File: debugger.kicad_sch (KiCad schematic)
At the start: 15 parts, among them J10 TC_SWD, J6 MCU_SWD, U6 ATSAMD11

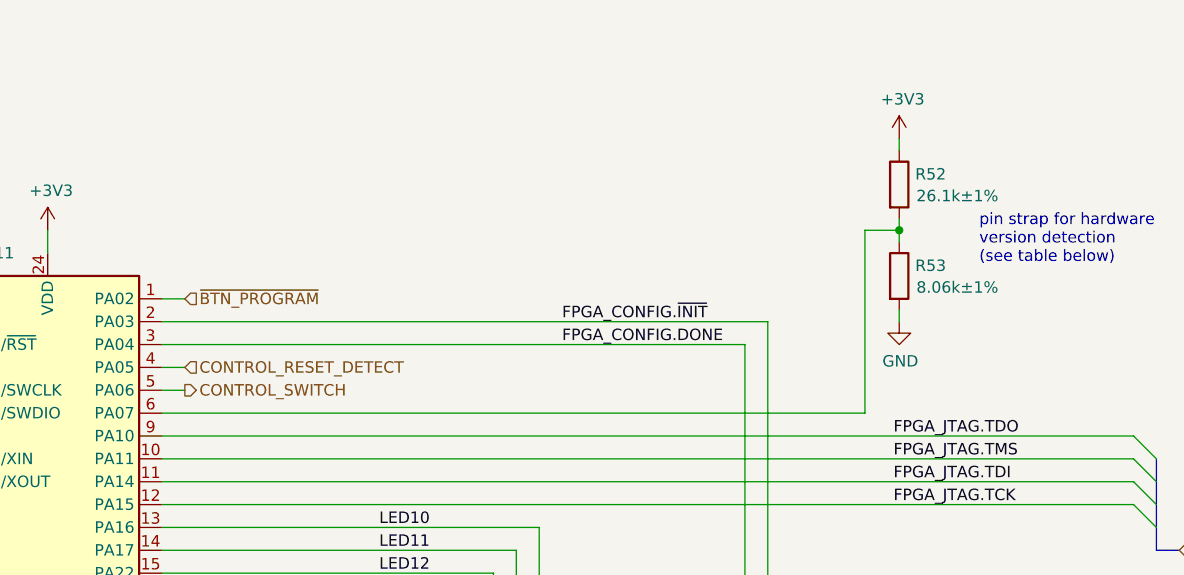
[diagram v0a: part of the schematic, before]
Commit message: Upgrade to KiCad 7
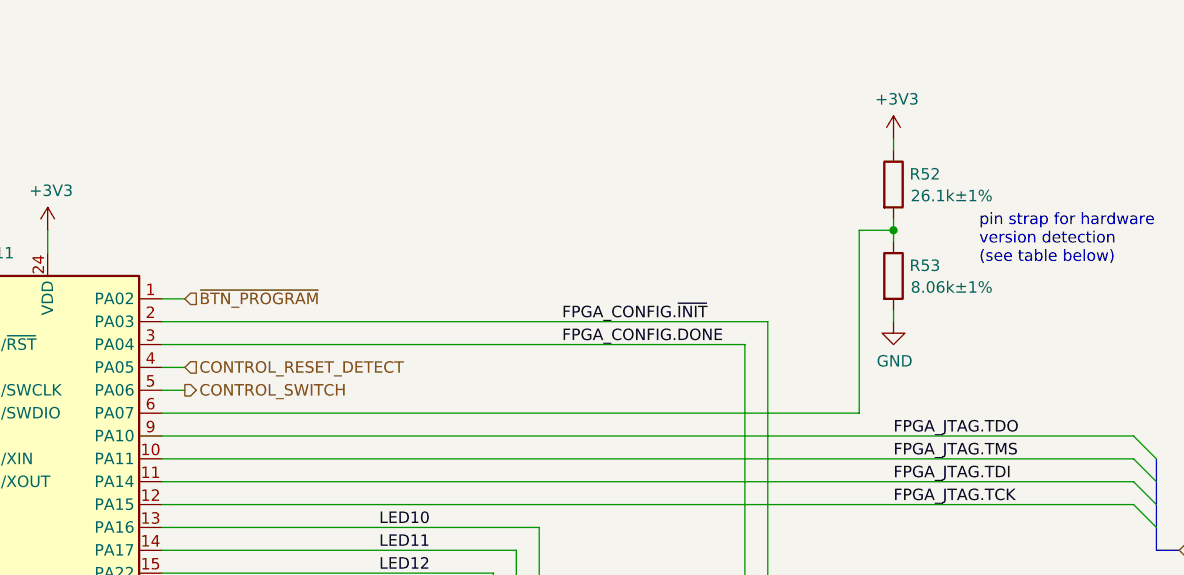
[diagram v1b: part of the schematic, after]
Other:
- moved on the sheet: R52, R53

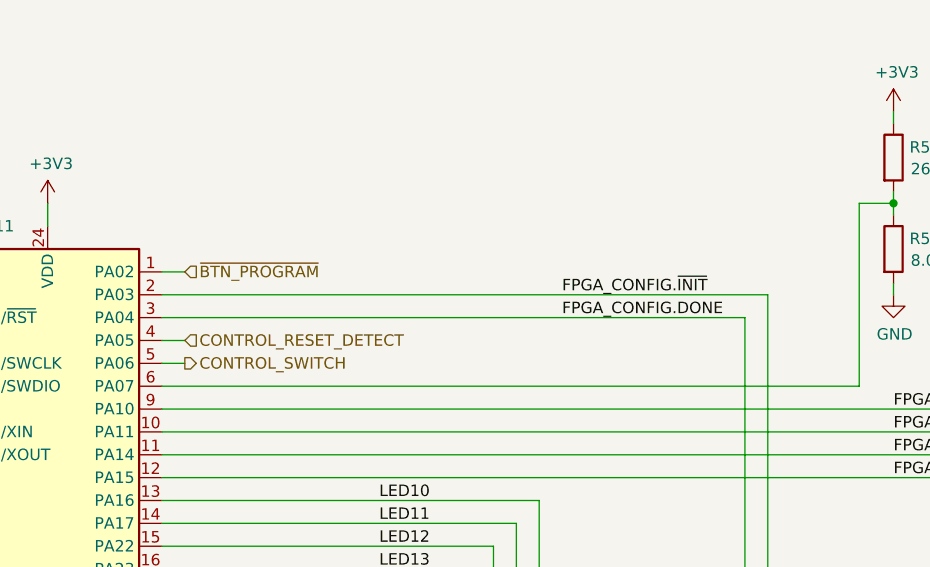
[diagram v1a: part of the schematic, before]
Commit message: Add FPGA_INIT (INITN) series resistor
Fixes #14
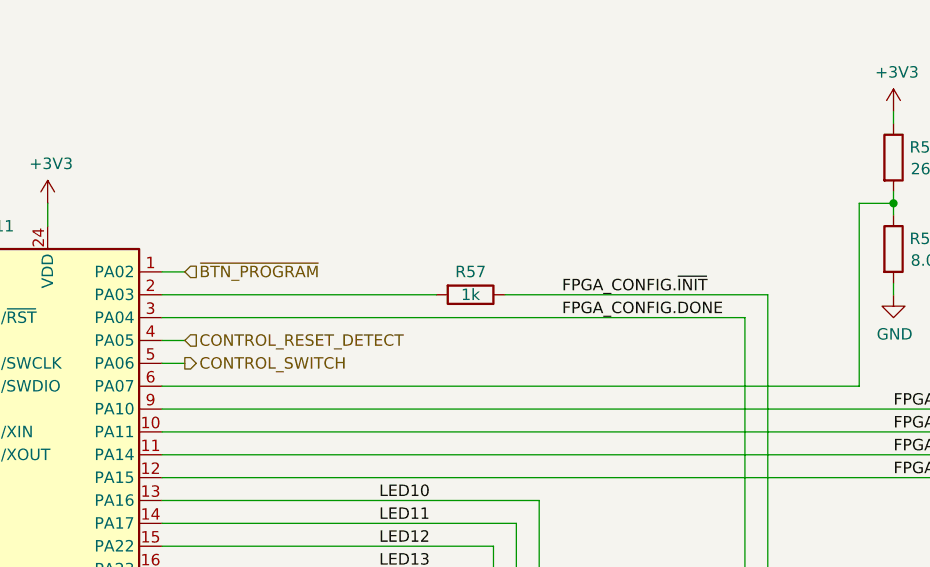
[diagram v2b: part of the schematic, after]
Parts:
- added R57: 1k, Resistor_SMD:R_0402_1005Metric, symbol Device:R
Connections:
- net FPGA_CONFIG.~{INIT}: now also R57.1; no longer U6.2 (PA03)
- new net: R57.2, U6.2 (PA03)
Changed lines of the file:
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@@
-    (stroke (width 0) (type default))
-  )
-  (wire (pts (xy 137.16 62.23) (xy 204.47 62.23))
     (stroke (width 0) (type default))
   )
@@
     (stroke (width 0) (type default))
   )
+  (wire (pts (xy 175.26 62.23) (xy 204.47 62.23))
+    (stroke (width 0) (type default))
+  )
   (wire (pts (xy 50.8 45.72) (xy 50.8 48.26))
     (stroke (width 0) (type default))
@@
   )
   (wire (pts (xy 60.96 48.26) (xy 63.5 48.26))
+    (stroke (width 0) (type default))
+  )
+  (wire (pts (xy 137.16 62.23) (xy 167.64 62.23))
     (stroke (width 0) (type default))
   )
@@
         )
       )
+    )
+  )
+  (symbol (lib_id "Device:R") (at 171.45 62.23 270) (unit 1)
+    (in_bom yes) (on_board yes) (dnp no)
+    (property "Reference" "R57" (at 171.45 59.69 90)
+      (effects (font (size 1.27 1.27)))
+    )
+    (property "Value" "1k" (at 171.45 62.23 90)
+      (effects (font (size 1.27 1.27)))
+    )
+    (property "Footprint" "Resistor_SMD:R_0402_1005Metric" (at 171.45 60.452 90)
+      (effects (font (size 1.27 1.27)) hide)
+    )
+    (property "Datasheet" "~" (at 171.45 62.23 0)
+      (effects (font (size 1.27 1.27)) hide)
+    )
+    (property "Part Number" "RC0402JR-071KL" (at 171.45 62.23 0)
+      (effects (font (size 1.27 1.27)) hide)
+    )
+    (property "Substitution" "any equivalent" (at 171.45 62.23 0)
+      (effects (font (size 1.27 1.27)) hide)
+    )
+    (property "Description" "RES 1K OHM 5% 1/16W 0402" (at 171.45 62.23 0)
+      (effects (font (size 1.27 1.27)) hide)
+    )
+    (property "Manufacturer" "Yageo" (at 171.45 62.23 0)
+      (effects (font (size 1.27 1.27)) hide)
+    )
+    (pin "1")
+    (pin "2")
+    (instances
+      (project "cynthion"
+        (path "/fb621148-8145-4217-9712-738e1b5a4823/00000000-0000-0000-0000-00005dddb747"
+          (reference "R57") (unit 1)
+        )
+        (path "/fb621148-8145-4217-9712-738e1b5a4823/00000000-0000-0000-0000-00005dcaa6d2"
+          (reference "R118") (unit 1)
+        )
+      )

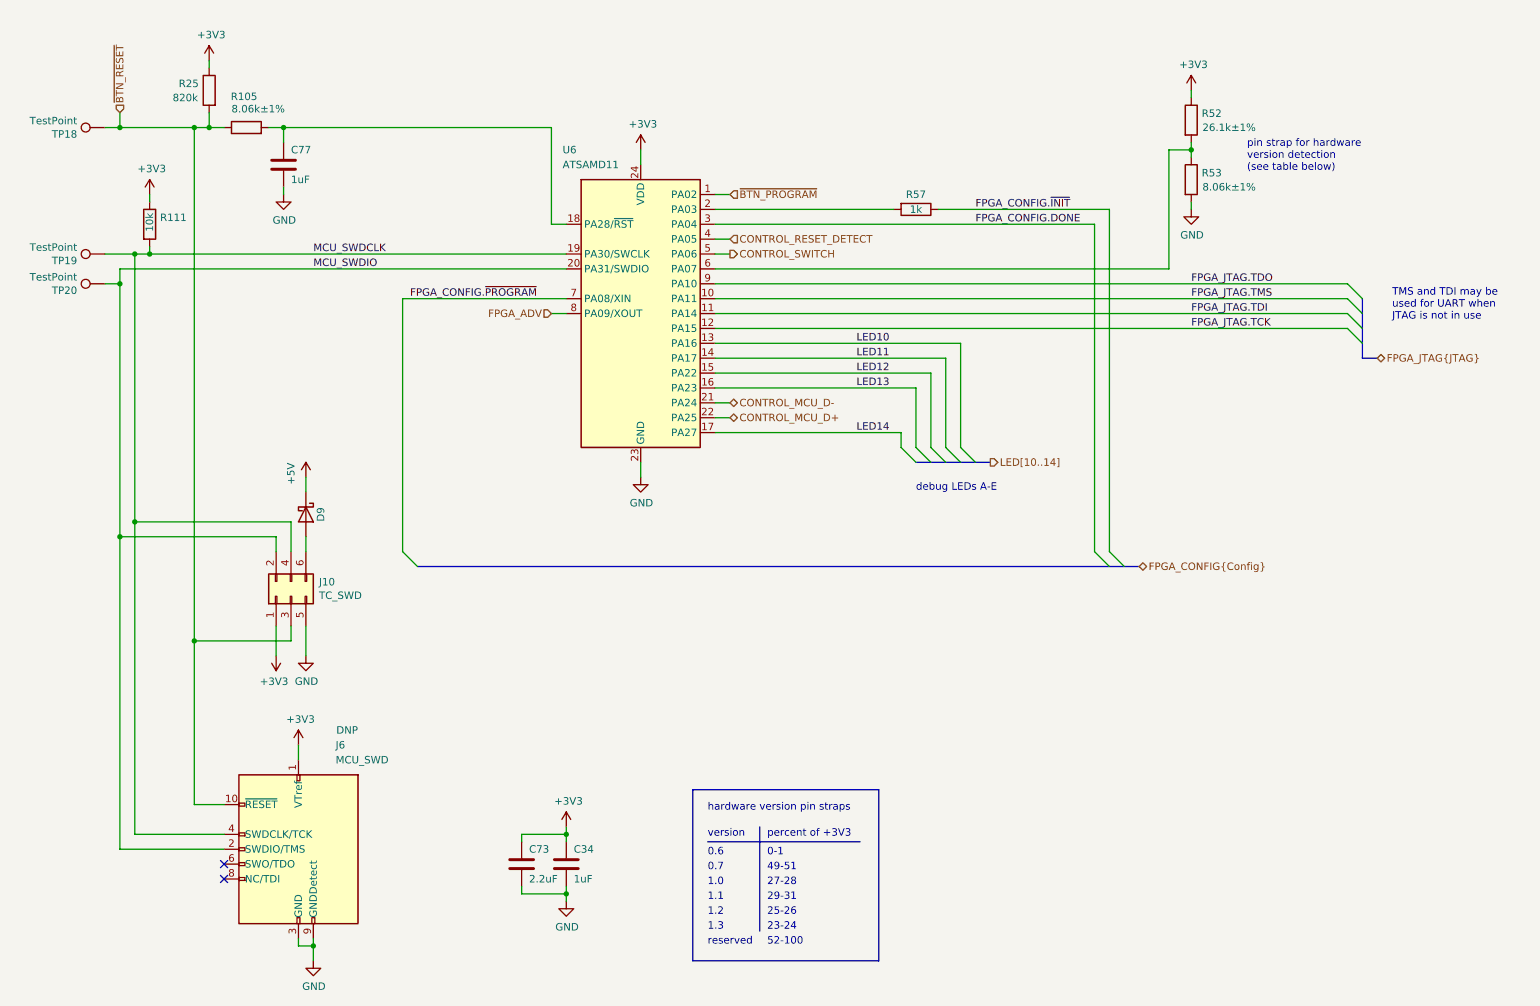
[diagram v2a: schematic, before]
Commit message: Clean up schematic
- Renumber Pmod signal names to match silkscreen labels
- Clean up FPGA symbol
- Clean up PHY symbol
- Add title block to newer sheets
- Fix horizontal line in LED sheet
- Improve various label positions
- Update data sheet fields
- Renumber pages
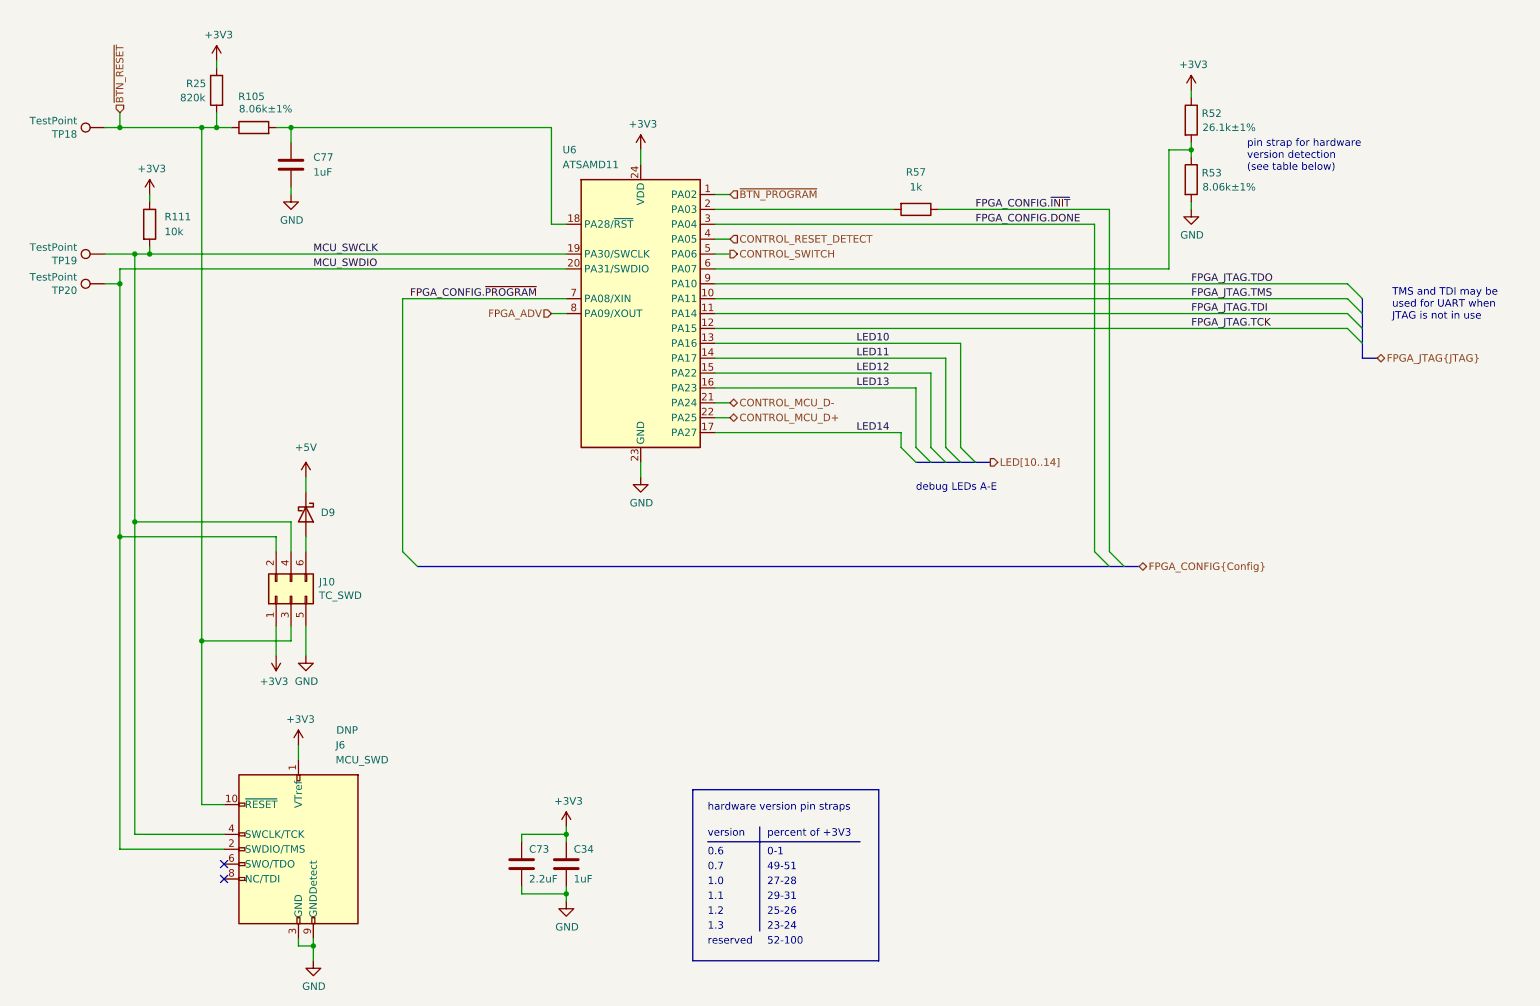
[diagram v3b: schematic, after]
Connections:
- net MCU_SWDCLK renamed MCU_SWCLK
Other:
- moved on the sheet: C77, R105, R25

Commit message: Update version detection pin strap
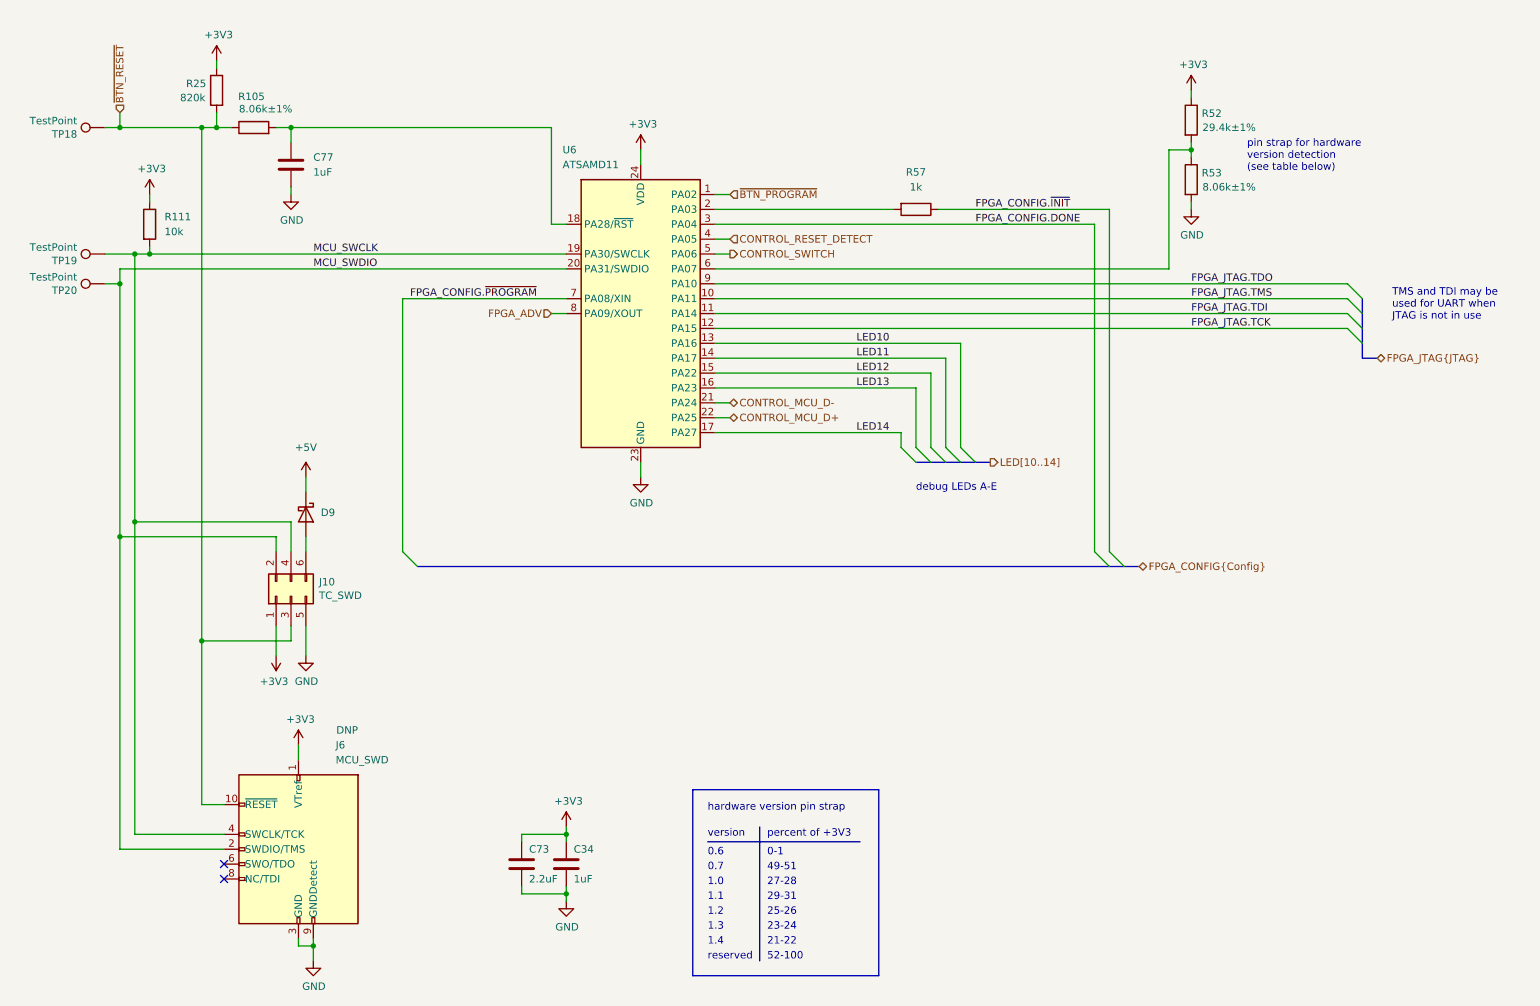
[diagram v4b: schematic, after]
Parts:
- R52: value 26.1k±1% -> 29.4k±1%; Part Number RC0402FR-0726K1L -> RC0402FR-0729K4L
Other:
- note added: "1.4"
- note added: "21-22"
- note added: "hardware version pin strap"
- note removed: "hardware version pin straps"
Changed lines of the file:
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@@
     (stroke (width 0) (type default))
   )
-  (polyline (pts (xy 133.35 161.29) (xy 133.35 190.5))
+  (polyline (pts (xy 133.35 161.29) (xy 133.35 193.04))
     (stroke (width 0) (type default))
   )
@@
     (stroke (width 0) (type default))
   )
-  (polyline (pts (xy 165.1 161.29) (xy 165.1 190.5))
+  (polyline (pts (xy 165.1 161.29) (xy 165.1 193.04))
     (stroke (width 0) (type default))
   )
@@
     (stroke (width 0) (type default))
   )
-  (polyline (pts (xy 165.1 190.5) (xy 133.35 190.5))
+  (polyline (pts (xy 165.1 193.04) (xy 133.35 193.04))
     (stroke (width 0) (type default))
   )
@@
     (stroke (width 0) (type default))
   )
-  (polyline (pts (xy 144.78 167.64) (xy 144.78 185.42))
+  (polyline (pts (xy 144.78 167.64) (xy 144.78 190.5))
     (stroke (width 0) (type default))
   )
@@
     (stroke (width 0) (type default))
   )
+  (text "1.4" (at 135.89 187.96 0)
+    (effects (font (size 1.27 1.27)) (justify left bottom))
+  )
   (text "debug LEDs A-E" (at 171.45 110.49 0)
     (effects (font (size 1.27 1.27)) (justify left bottom))
   )
-  (text "reserved" (at 135.89 187.96 0)
+  (text "reserved" (at 135.89 190.5 0)
     (effects (font (size 1.27 1.27)) (justify left bottom))
   )
@@
     (effects (font (size 1.27 1.27)) (justify left bottom))
   )
-  (text "52-100" (at 146.05 187.96 0)
+  (text "52-100" (at 146.05 190.5 0)
     (effects (font (size 1.27 1.27)) (justify left bottom))
   )
@@
     (effects (font (size 1.27 1.27)) (justify left bottom))
   )
+  (text "21-22" (at 146.05 187.96 0)
+    (effects (font (size 1.27 1.27)) (justify left bottom))
+  )
   (text "1.1" (at 135.89 180.34 0)
     (effects (font (size 1.27 1.27)) (justify left bottom))
   )
-  (text "hardware version pin straps" (at 135.89 165.1 0)
+  (text "hardware version pin strap" (at 135.89 165.1 0)
     (effects (font (size 1.27 1.27)) (justify left bottom))
   )
@@
       (effects (font (size 1.27 1.27)) (justify left))
     )
-    (property "Value" "26.1k±1%" (at 220.345 48.26 0)
+    (property "Value" "29.4k±1%" (at 220.345 48.26 0)
       (effects (font (size 1.27 1.27)) (justify left))
     )
@@
       (effects (font (size 1.27 1.27)) hide)
     )
-    (property "Part Number" "RC0402FR-0726K1L" (at 218.44 46.99 0)
+    (property "Part Number" "RC0402FR-0729K4L" (at 218.44 46.99 0)
       (effects (font (size 1.27 1.27)) hide)
     )
@@
       (effects (font (size 1.27 1.27)) hide)
     )
-    (property "Description" "RES 26.1K OHM 1% 1/16W 0402" (at 218.44 46.99 0)
-      (effects (font (size 1.27 1.27)) hide)
-    )
+    (property "Description" "RES 29.4K OHM 1% 1/16W 0402" (at 218.44 46.99 0)
+      (effects (font (size 1.27 1.27)) hide)
+    )

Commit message: opened and saved in KiCad 7.0.10
after upgrading from 7.0.9
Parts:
- renumbered R57 to R118
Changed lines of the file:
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@@
   (symbol (lib_id "Device:R") (at 171.45 62.23 270) (unit 1)
     (in_bom yes) (on_board yes) (dnp no) (fields_autoplaced)
-    (property "Reference" "R57" (at 171.45 55.88 90)
+    (property "Reference" "R118" (at 171.45 55.88 90)
       (effects (font (size 1.27 1.27)))
     )
@@
     (instances
       (project "cynthion"
-        (path "/fb621148-8145-4217-9712-738e1b5a4823/00000000-0000-0000-0000-00005dddb747"
-          (reference "R57") (unit 1)
-        )
         (path "/fb621148-8145-4217-9712-738e1b5a4823/00000000-0000-0000-0000-00005dcaa6d2"
           (reference "R118") (unit 1)

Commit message: Update copyright notices
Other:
- company: Copyright 2019-2023 Great Scott Gadgets -> ${COPYRIGHT}
- title: Cynthion -> ${TITLE}
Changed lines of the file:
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@@
   (paper "A4")
   (title_block
-    (title "Cynthion")
+    (title "${TITLE}")
     (date "${DATE}")
     (rev "${VERSION}")
-    (company "Copyright 2019-2023 Great Scott Gadgets")
-    (comment 1 "Licensed under the CERN-OHL-P v2")
+    (company "${COPYRIGHT}")
+    (comment 1 "${LICENSE}")
   )
   (junction (at 52.07 48.26) (diameter 0) (color 0 0 0 0)
